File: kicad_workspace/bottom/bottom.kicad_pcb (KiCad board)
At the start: 2 copper layers, 76.8 x 84 mm, 37 parts, among them J1 Battery connector, J2 Battery connector, M1 N20_MOTOR_EXTENDED_SHAFT, M2 N20_MOTOR_EXTENDED_SHAFT, U1 DRV8833PWP, U3 ATmega4809-A, U4 BNO055, Y1 32.768kHz

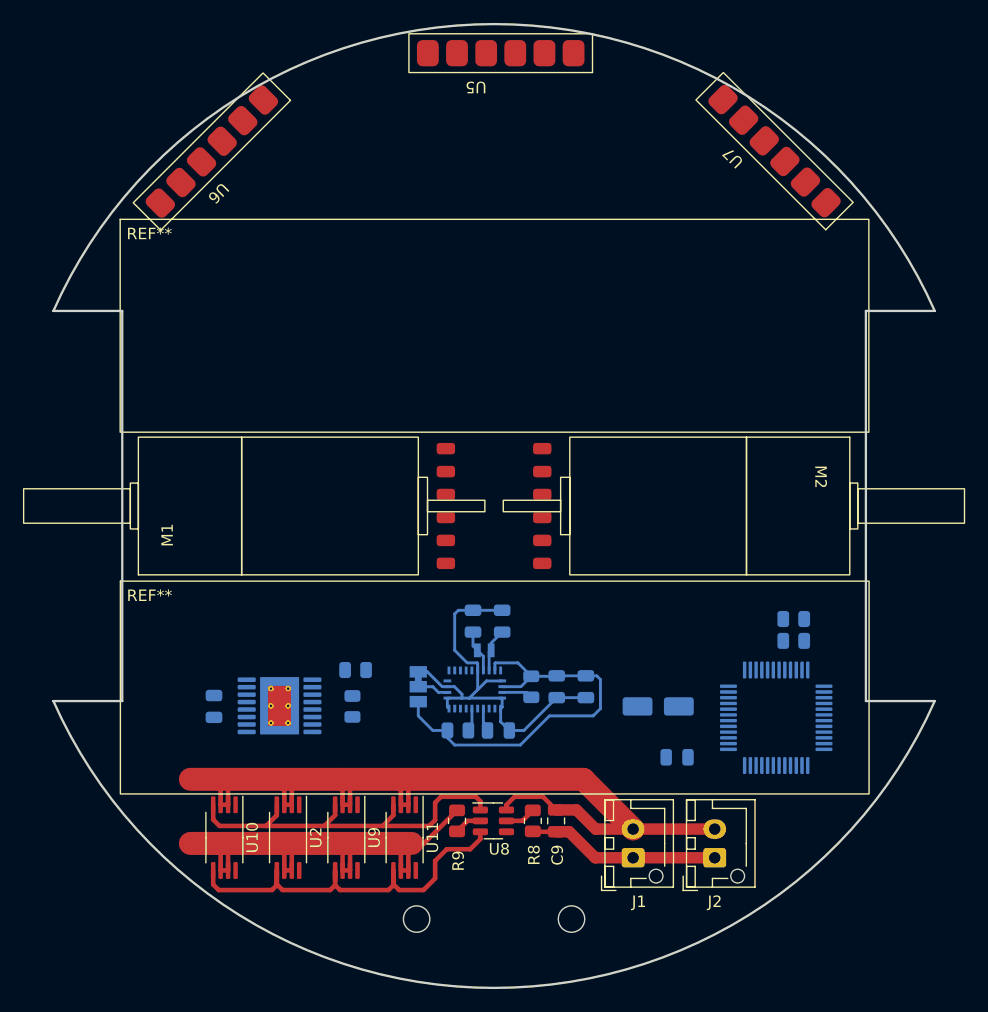
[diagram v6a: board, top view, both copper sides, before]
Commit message: initial stm and its elements placement
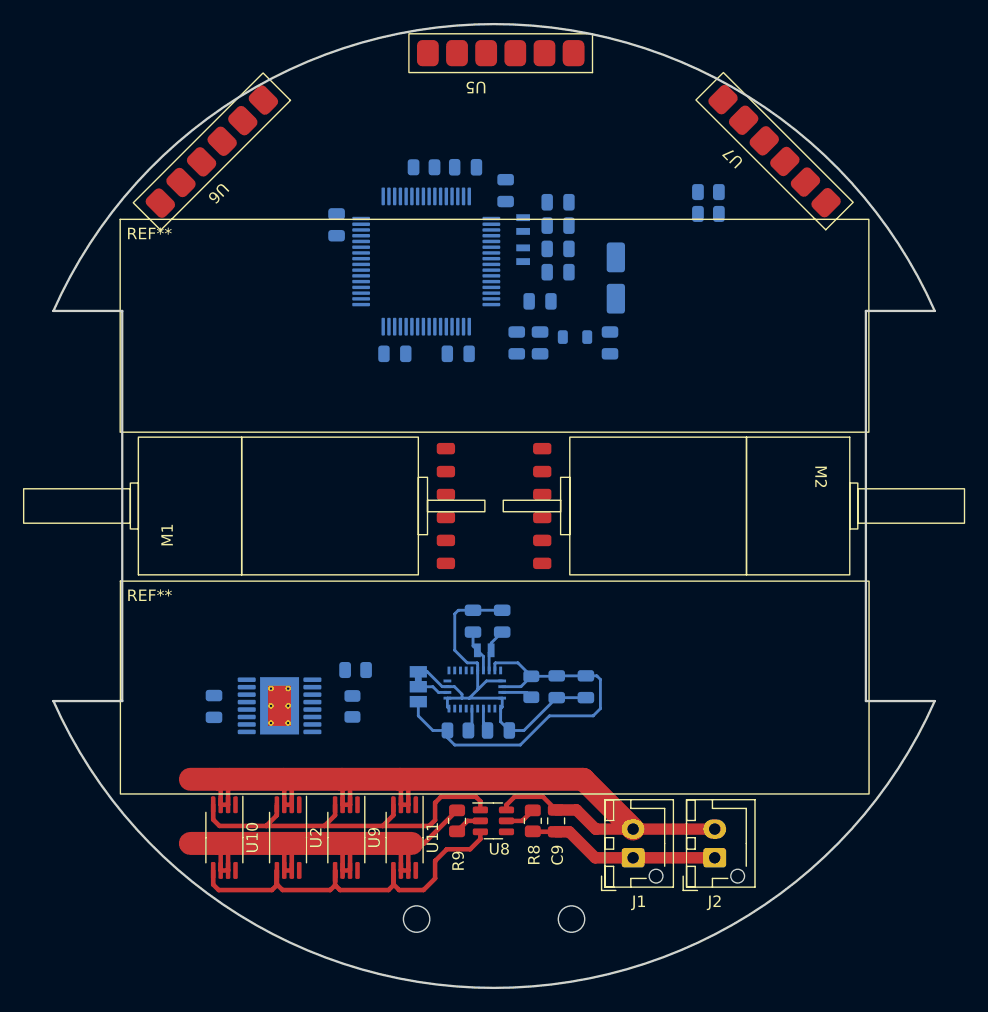
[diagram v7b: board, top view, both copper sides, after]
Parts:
- added C10: 100nF, Capacitor_SMD:C_0805_2012Metric, B.Cu at (64.0, 42.2)
- added C11: 1uF, Capacitor_SMD:C_0805_2012Metric, B.Cu at (61.0, 32.5)
- added C12: 100nF, Capacitor_SMD:C_0805_2012Metric, B.Cu at (46.3, 35.5)
- added C13: 100nF, Capacitor_SMD:C_0805_2012Metric, B.Cu at (51.4, 46.7)
- added C14: 100nF, Capacitor_SMD:C_0805_2012Metric, B.Cu at (56.9, 46.7)
- added C15: 100nF, Capacitor_SMD:C_0805_2012Metric, B.Cu at (57.5, 30.5)
- added C16: 1uF, Capacitor_SMD:C_0805_2012Metric, B.Cu at (64.0, 45.8)
- added C17: 10nF, Capacitor_SMD:C_0805_2012Metric, B.Cu at (62.0, 45.8)
- added C18: 12pf, Capacitor_SMD:C_0805_2012Metric, B.Cu at (65.6, 39.6)
- added C19: 12pf, Capacitor_SMD:C_0805_2012Metric, B.Cu at (65.6, 37.6)
- added C20: 4.3pF, Capacitor_SMD:C_0805_2012Metric, B.Cu at (65.6, 35.6)
- added C21: 4.3pF, Capacitor_SMD:C_0805_2012Metric, B.Cu at (65.6, 33.5)
- added FB1: FerriteBead, Inductor_SMD:L_0805_2012Metric, B.Cu at (67.1, 45.3)
- added R3: 10K, Resistor_SMD:R_0805_2012Metric, B.Cu at (53.9, 30.5)
- added Y2: 8MHz, Crystal:Crystal_SMD_MicroCrystal_CM9V-T1A-2Pin_1.6x1.0mm, B.Cu at (62.5, 38.1)
- added Y3: 32.768kHz, Crystal:Crystal_SMD_MicroCrystal_CM9V-T1A-2Pin_1.6x1.0mm, B.Cu at (62.5, 35.5)
- C2: value 100nF -> 1uF
- U3: value ATmega4809-A -> STM32F303RETx; footprint Package_QFP:TQFP-48_7x7mm_P0.5mm -> Package_QFP:LQFP-64_10x10mm_P0.5mm
- moved U3 50.1 mm to (54.1, 38.7)
- moved R7 37.9 mm to (78.7, 34.5)
- moved R6 37.9 mm to (78.7, 32.6)
- moved C3 37.5 mm to (70.6, 40.1), turned to 90 degrees
- moved C2 36.6 mm to (70.1, 45.8), turned to -90 degrees
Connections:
- U3 pad 1: unconnected-(U3-PA5-Pad1) -> +3.3V
- U3 pad 10: VL_EN1 -> DRV_B1
- U3 pad 11: VL_EN2 -> DRV_B2
- U3 pad 12: VL_EN3 -> GND
- U3 pad 13: unconnected-(U3-PC3-Pad13) -> +3.3VA
- U3 pad 14: +3.3V -> unconnected-(U3-PA0-Pad14)
- U3 pad 15: GND -> unconnected-(U3-PA1-Pad15)
- U3 pad 18: unconnected-(U3-PC6-Pad18) -> GND
- U3 pad 19: unconnected-(U3-PC7-Pad19) -> +3.3V
- U3 pad 26: unconnected-(U3-PD6-Pad26) -> M1_A
- U3 pad 27: unconnected-(U3-PD7-Pad27) -> M1_B
- U3 pad 28: +3.3V -> M2_A
- U3 pad 29: GND -> BNO_INT
- U3 pad 3: BNO_INT -> Net-(U3-PC14)
- U3 pad 31: unconnected-(U3-PE1-Pad31) -> GND
- U3 pad 32: unconnected-(U3-PE2-Pad32) -> +3.3V
- U3 pad 34: DRV_A1 -> unconnected-(U3-PB13-Pad34)
- U3 pad 35: DRV_A2 -> unconnected-(U3-PB14-Pad35)
- U3 pad 36: DRV_B1 -> unconnected-(U3-PB15-Pad36)
- U3 pad 37: DRV_B2 -> unconnected-(U3-PC6-Pad37)
- U3 pad 4: M1_A -> Net-(U3-PC15)
- U3 pad 41: unconnected-(U3-UPDI-Pad41) -> SDA
- U3 pad 42: +3.3V -> SCL
- U3 pad 43: GND -> unconnected-(U3-PA10-Pad43)
- U3 pad 46: SDA -> unconnected-(U3-PA13-Pad46)
- U3 pad 47: SCL -> GND
- U3 pad 48: unconnected-(U3-PA4-Pad48) -> +3.3V
- U3 pad 5: M1_B -> Net-(U3-PF0)
- U3 pad 6: M2_A -> Net-(U3-PF1)
- U3 pad 7: M2_B -> /NRST
- U3 pad 8: unconnected-(U3-PB4-Pad8) -> DRV_A1
- U3 pad 9: unconnected-(U3-PB5-Pad9) -> DRV_A2
